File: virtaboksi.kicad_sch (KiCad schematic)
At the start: 33 parts, among them J1 Panel_01x06, J2 External_01x06, J3 Optional_01x03, J5 Powerpole 01x02, J6 Powerpole 01x02, J7 Powerpole 01x02, J8 TagConnect_TC2030-NL, Q10 MMBT3906, Q11 MMBT3906, Q12 MMBT3906, Q13 MMBT3906, U1 SRV05-4, U2 AMSRI-783.3-NZ, U3 SRV05-4, U4 SP3485EN, U5 STM8S003F3P

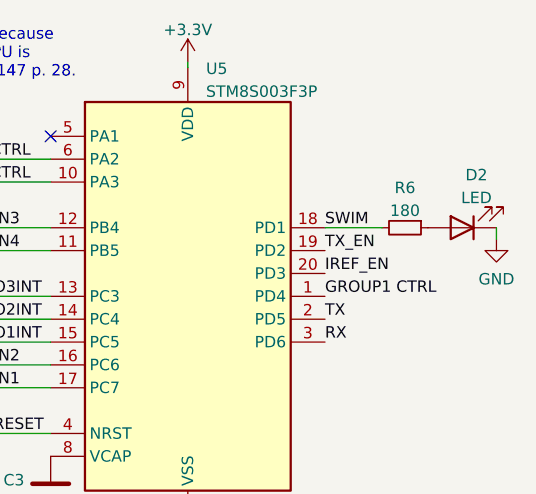
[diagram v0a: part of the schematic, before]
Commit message: Move labels, change on-board LED resistor from 180 ohm to 220
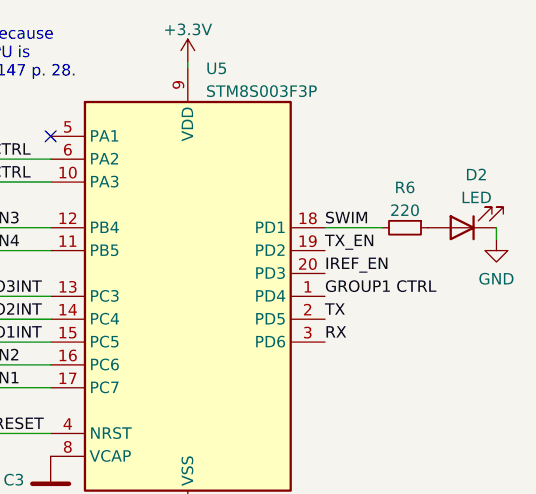
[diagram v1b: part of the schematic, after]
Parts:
- R6: value 180 -> 220; LCSC C22828 -> C22962
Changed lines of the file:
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@@
     (in_bom yes) (on_board yes)
     (property "Reference" "R6" (id 0) (at 270.51 34.9336 90))
-    (property "Value" "180" (id 1) (at 270.51 37.4705 90))
+    (property "Value" "220" (id 1) (at 270.51 37.4705 90))
     (property "Footprint" "Resistor_SMD:R_0603_1608Metric" (id 2) (at 270.51 39.37 0)
       (effects (font (size 1.27 1.27)) hide)
@@
       (effects (font (size 1.27 1.27)) hide)
     )
-    (property "LCSC" "C22828" (id 4) (at 270.51 39.37 0)
+    (property "LCSC" "C22962" (id 4) (at 270.51 39.37 0)
       (effects (font (size 1.27 1.27)) hide)
     )
@@
     )
     (path "/4abc25c1-7ff8-4306-84ab-5eb54e1905de"
-      (reference "R6") (unit 1) (value "180") (footprint "Resistor_SMD:R_0603_1608Metric")
+      (reference "R6") (unit 1) (value "220") (footprint "Resistor_SMD:R_0603_1608Metric")
     )
     (path "/148741a4-2a3a-400f-b0f5-c870db1d25a5/0a9b5501-e006-44fb-b6b0-34558cc042ce"

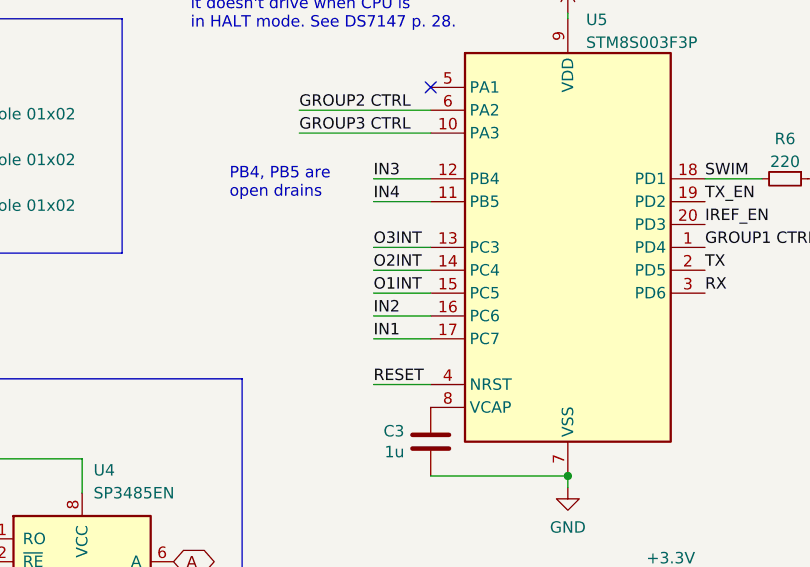
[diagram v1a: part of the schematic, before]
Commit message: Move AIN4 pin to IN2 to make it possible to use it for analog in the future
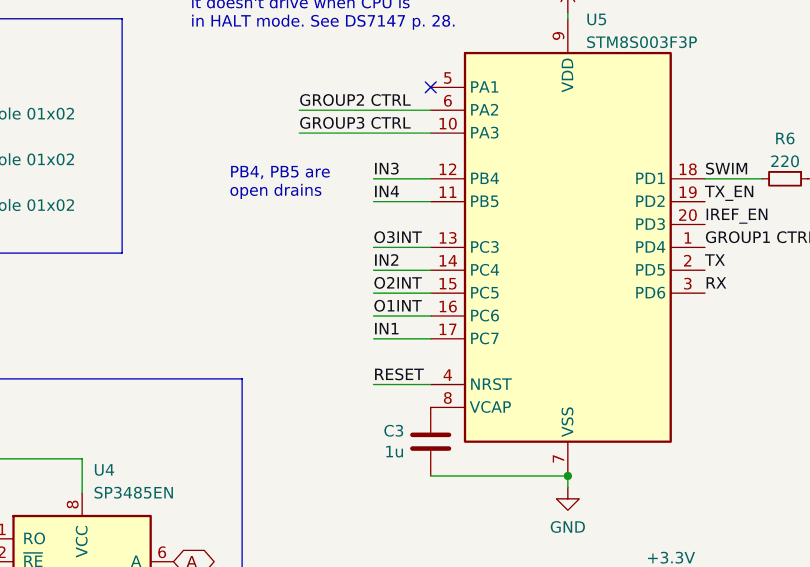
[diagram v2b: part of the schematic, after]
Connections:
- net IN2: now also U5.14 (PC4); no longer U5.16 (PC6)
- net O1INT: now also U5.16 (PC6); no longer U5.15 (PC5)
- net O2INT: now also U5.15 (PC5); no longer U5.14 (PC4)
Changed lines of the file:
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@@
     (effects (font (size 1.27 1.27)) (justify left bottom))
   )
-  (label "O1INT" (at 224.79 52.07 0)
+  (label "O1INT" (at 224.79 54.61 0)
     (effects (font (size 1.27 1.27)) (justify left bottom))
   )
@@
     (effects (font (size 1.27 1.27)) (justify left bottom))
   )
-  (label "IN2" (at 224.79 54.61 0)
+  (label "IN2" (at 224.79 49.53 0)
     (effects (font (size 1.27 1.27)) (justify left bottom))
   )
@@
     (effects (font (size 1.27 1.27)) (justify left bottom))
   )
-  (label "O2INT" (at 224.79 49.53 0)
+  (label "O2INT" (at 224.79 52.07 0)
     (effects (font (size 1.27 1.27)) (justify left bottom))
   )

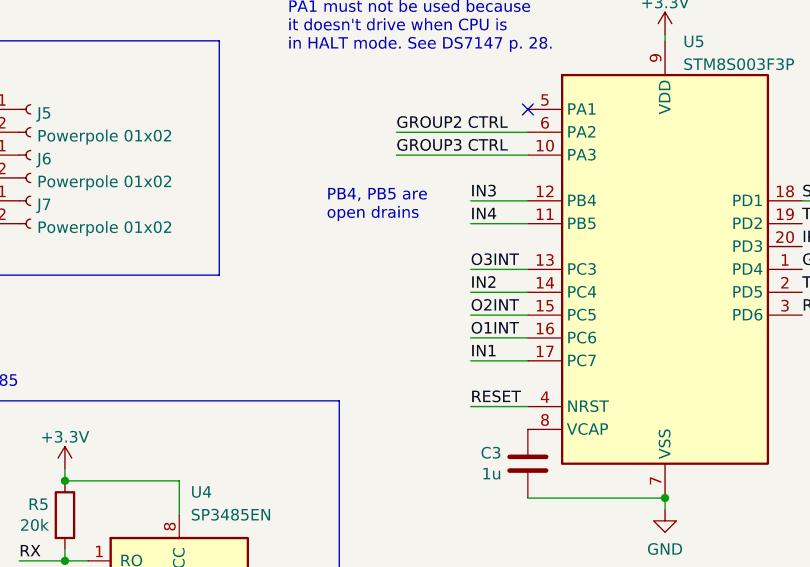
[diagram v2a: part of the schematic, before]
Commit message: Add a label mentioning about analog use
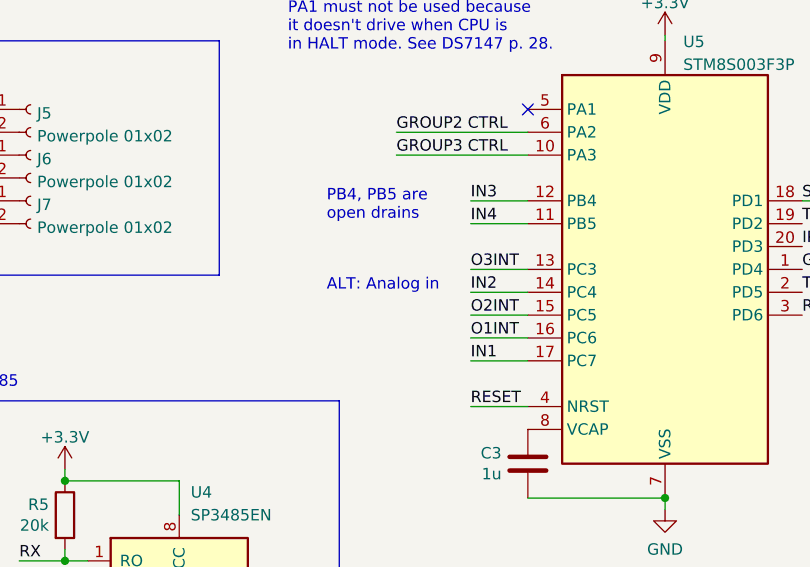
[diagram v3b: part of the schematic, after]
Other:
- note added: "ALT: Analog in"
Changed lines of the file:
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@@
+    (effects (font (size 1.27 1.27)) (justify left bottom))
+  )
+  (text "ALT: Analog in" (at 208.788 49.53 0)
     (effects (font (size 1.27 1.27)) (justify left bottom))
   )

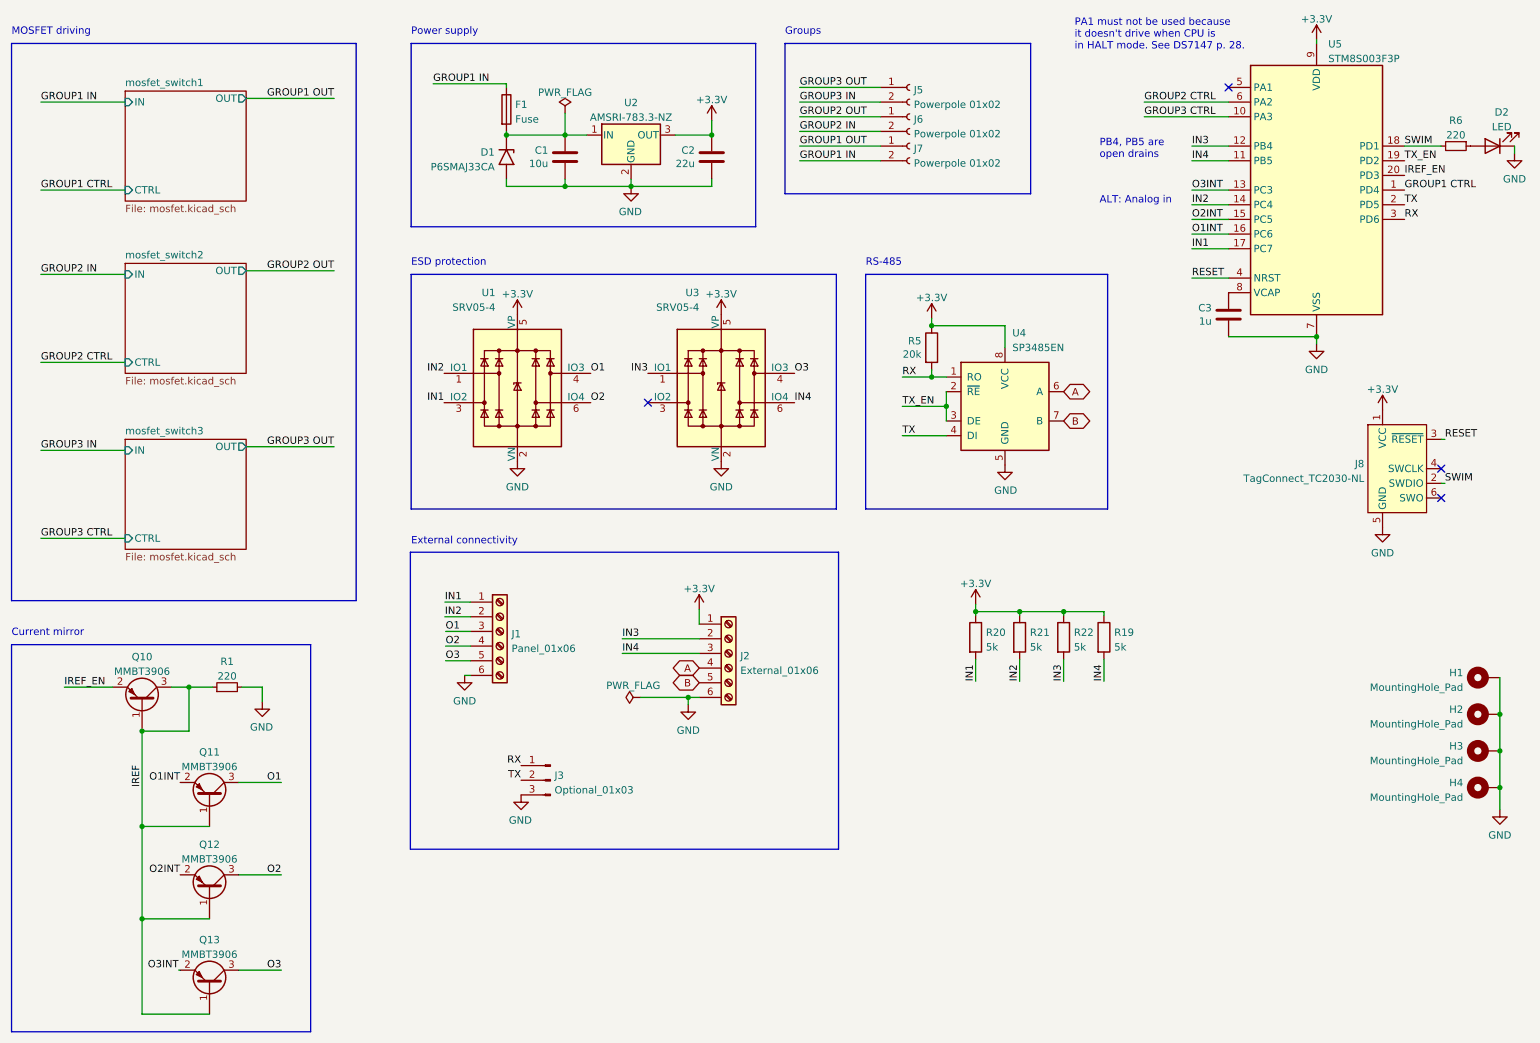
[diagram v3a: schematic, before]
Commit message: Small tweaks such as renaming OxINT to OxuC
Old name confused because INT is often interrupt
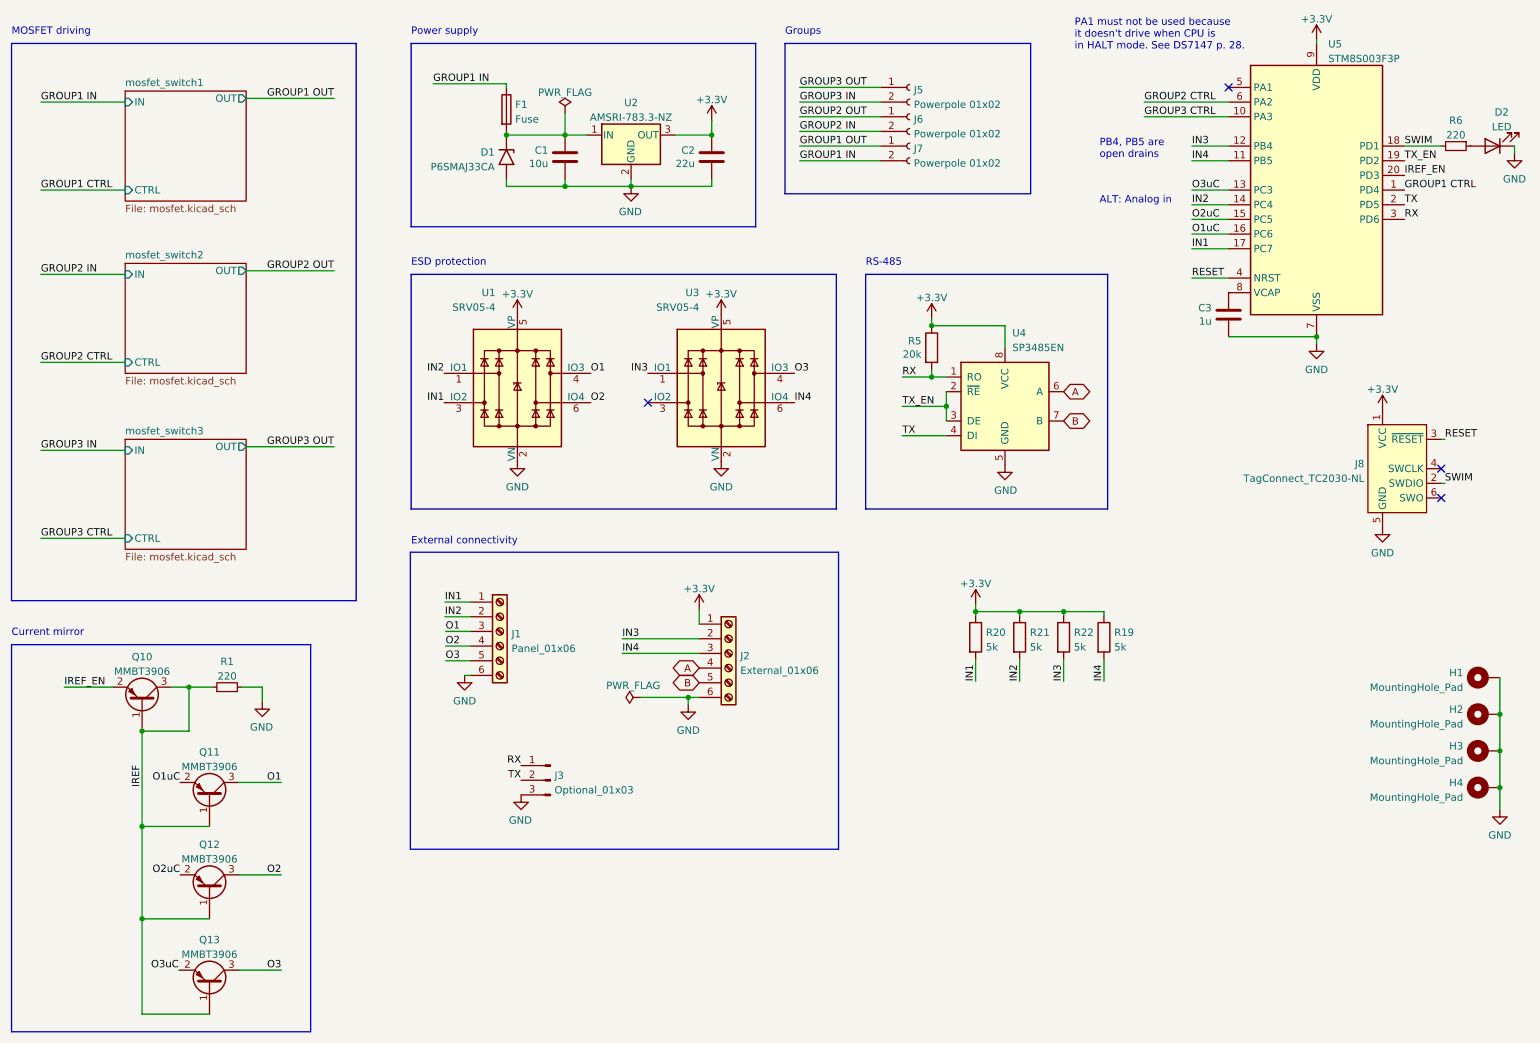
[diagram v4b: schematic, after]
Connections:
- net O1INT renamed O1uC
- net O2INT renamed O2uC
- net O3INT renamed O3uC
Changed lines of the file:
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@@
     (effects (font (size 1.27 1.27)) (justify left bottom))
   )
-  (label "O1INT" (at 224.79 54.61 0)
+  (label "O1uC" (at 224.79 54.61 0)
     (effects (font (size 1.27 1.27)) (justify left bottom))
   )
@@
     (effects (font (size 1.27 1.27)) (justify left bottom))
   )
-  (label "O2INT" (at 49.53 165.608 180)
+  (label "O2uC" (at 49.53 165.608 180)
     (effects (font (size 1.27 1.27)) (justify right bottom))
   )
@@
     (effects (font (size 1.27 1.27)) (justify left bottom))
   )
-  (label "O3INT" (at 49.276 182.118 180)
+  (label "O3uC" (at 49.276 182.118 180)
     (effects (font (size 1.27 1.27)) (justify right bottom))
   )
@@
     (effects (font (size 1.27 1.27)) (justify left bottom))
   )
-  (label "O3INT" (at 224.79 46.99 0)
+  (label "O3uC" (at 224.79 46.99 0)
     (effects (font (size 1.27 1.27)) (justify left bottom))
   )
@@
     (effects (font (size 1.27 1.27)) (justify left bottom))
   )
-  (label "O2INT" (at 224.79 52.07 0)
+  (label "O2uC" (at 224.79 52.07 0)
     (effects (font (size 1.27 1.27)) (justify left bottom))
   )
@@
     (effects (font (size 1.27 1.27)) (justify left bottom))
   )
-  (label "O1INT" (at 49.53 149.606 180)
+  (label "O1uC" (at 49.53 149.606 180)
     (effects (font (size 1.27 1.27)) (justify right bottom))
   )

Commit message: Incorrect part number spotted before production, 1.5kohm -> 4.7kohm
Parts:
- R19, R20, R21, R22: LCSC C22843 -> C23162
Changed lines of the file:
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@@
       (effects (font (size 1.27 1.27)) hide)
     )
-    (property "LCSC" "C22843" (id 4) (at 194.945 124.46 0)
+    (property "LCSC" "C23162" (id 4) (at 194.945 124.46 0)
       (effects (font (size 1.27 1.27)) hide)
     )
@@
       (effects (font (size 1.27 1.27)) hide)
     )
-    (property "LCSC" "C22843" (id 4) (at 209.55 124.46 0)
+    (property "LCSC" "C23162" (id 4) (at 209.55 124.46 0)
       (effects (font (size 1.27 1.27)) hide)
     )
@@
       (effects (font (size 1.27 1.27)) hide)
     )
-    (property "LCSC" "C22843" (id 4) (at 187.325 124.46 0)
+    (property "LCSC" "C23162" (id 4) (at 187.325 124.46 0)
       (effects (font (size 1.27 1.27)) hide)
     )
@@
       (effects (font (size 1.27 1.27)) hide)
     )
-    (property "LCSC" "C22843" (id 4) (at 202.565 124.46 0)
-      (effects (font (size 1.27 1.27)) hide)
-    )
+    (property "LCSC" "C23162" (id 4) (at 202.565 124.46 0)
+      (effects (font (size 1.27 1.27)) hide)
+    )

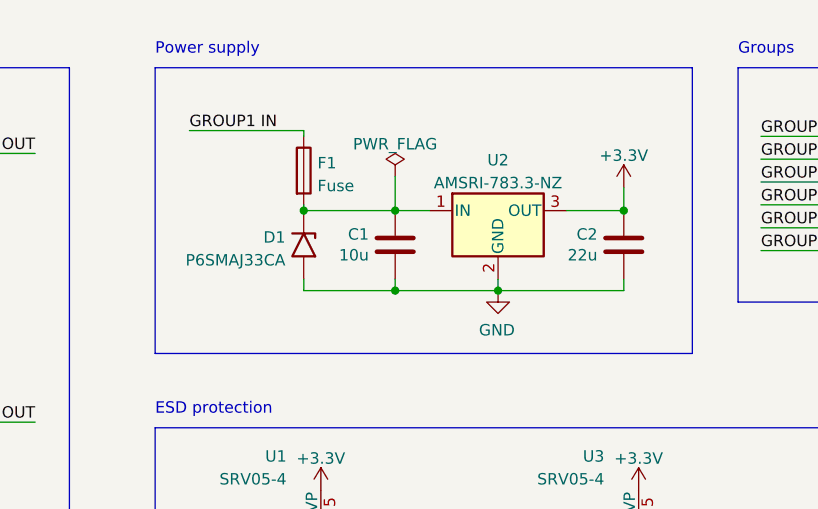
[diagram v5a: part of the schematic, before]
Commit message: Make clearance larger for power lines and relief smaller for ground (both now 0.4mm)
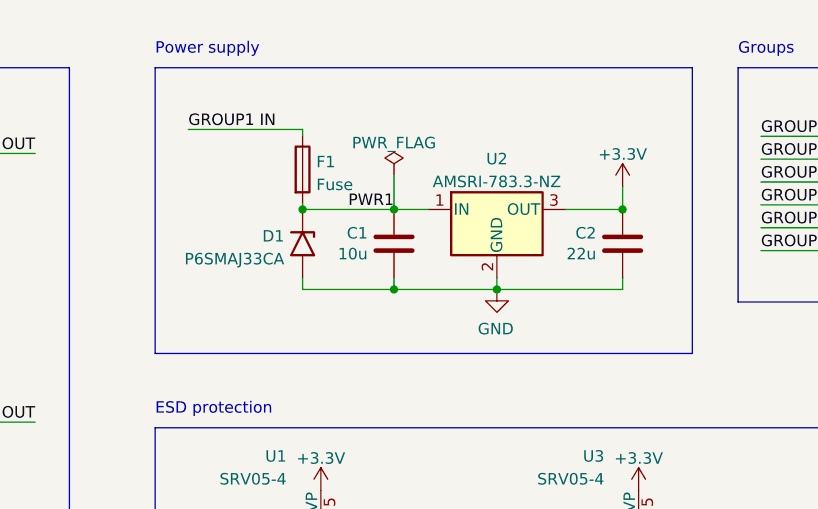
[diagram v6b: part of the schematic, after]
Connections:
- net PWR1: now reaches C1.1, D1.1 (A1), F1.2, U2.1 (IN)

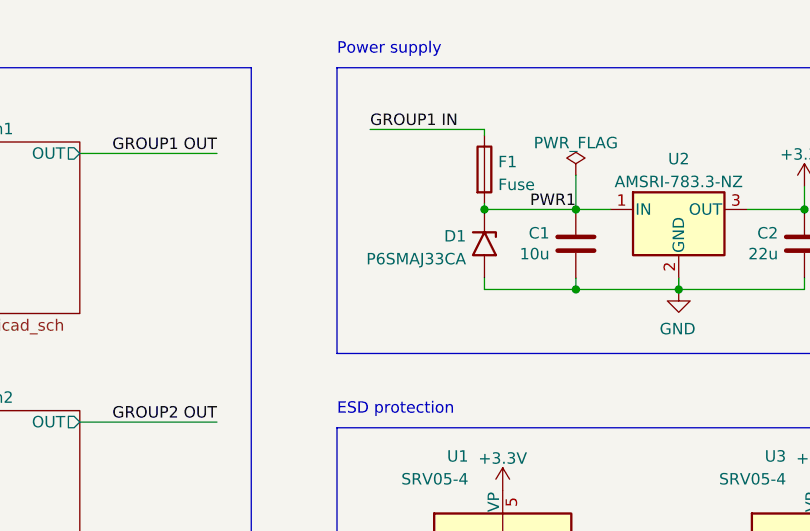
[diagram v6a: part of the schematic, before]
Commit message: Change bidirectional TVS to unidirectional
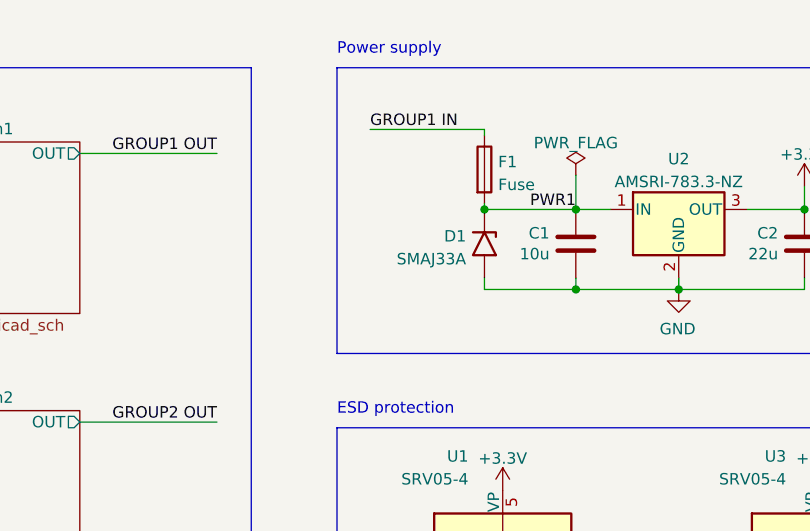
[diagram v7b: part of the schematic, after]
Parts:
- D1: value P6SMAJ33CA -> SMAJ33A; LCSC C3019524 -> C353454
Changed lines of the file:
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@@
   (symbol (lib_id "Diode:SMF30A") (at 105.918 41.148 270) (unit 1)
     (in_bom yes) (on_board yes) (fields_autoplaced)
-    (property "Reference" "D1" (id 0) (at 103.8861 40.3133 90)
-      (effects (font (size 1.27 1.27)) (justify right))
-    )
-    (property "Value" "P6SMAJ33CA" (id 1) (at 103.8861 42.8502 90)
+    (property "Reference" "D1" (id 0) (at 103.886 40.3133 90)
+      (effects (font (size 1.27 1.27)) (justify right))
+    )
+    (property "Value" "SMAJ33A" (id 1) (at 103.886 42.8502 90)
       (effects (font (size 1.27 1.27)) (justify right))
     )
@@
       (effects (font (size 1.27 1.27)) hide)
     )
-    (property "Datasheet" "https://datasheet.lcsc.com/lcsc/2205231816_Liown-P6SMAJ33CA_C3019524.pdf" (id 3) (at 105.918 39.878 0)
-      (effects (font (size 1.27 1.27)) hide)
-    )
-    (property "LCSC" "C3019524" (id 4) (at 105.918 41.148 90)
+    (property "Datasheet" "https://datasheet.lcsc.com/lcsc/2304140030_Shandong-Jingdao-Microelectronics-SMAJ33A_C353454.pdf" (id 3) (at 105.918 39.878 0)
+      (effects (font (size 1.27 1.27)) hide)
+    )
+    (property "LCSC" "C353454" (id 4) (at 105.918 41.148 90)
       (effects (font (size 1.27 1.27)) hide)
     )
@@
     )
     (path "/b067f70b-edd4-44a2-8814-61bf0ed84a1b"
-      (reference "D1") (unit 1) (value "P6SMAJ33CA") (footprint "Diode_SMD:D_SMA_Handsoldering")
+      (reference "D1") (unit 1) (value "SMAJ33A") (footprint "Diode_SMD:D_SMA_Handsoldering")
     )
     (path "/656e4e66-906f-41f9-990e-6c1e3b825465"
